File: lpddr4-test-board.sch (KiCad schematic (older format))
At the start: 0 parts

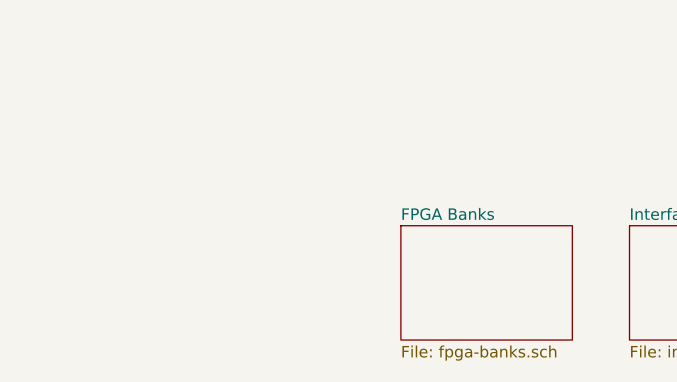
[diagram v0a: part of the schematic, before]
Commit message: Added HyperRAM
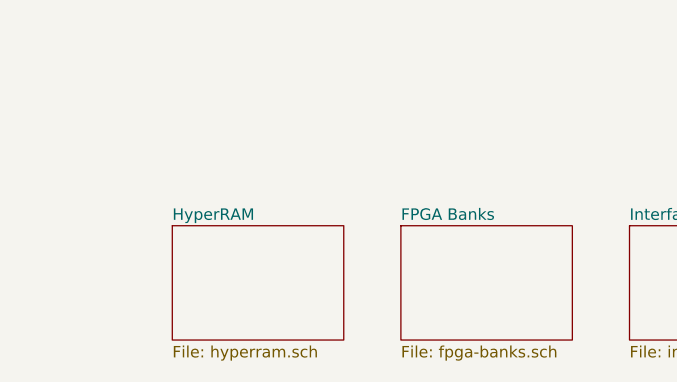
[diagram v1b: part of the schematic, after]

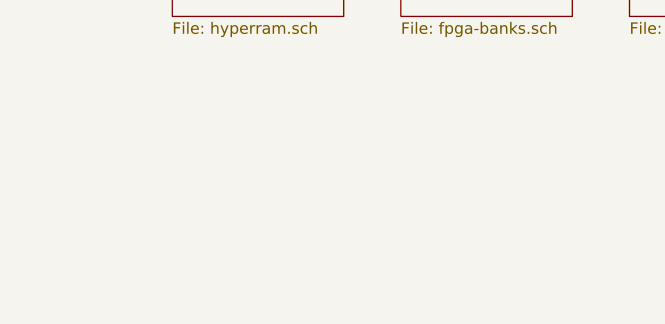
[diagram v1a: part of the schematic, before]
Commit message: Add OSHW logotype
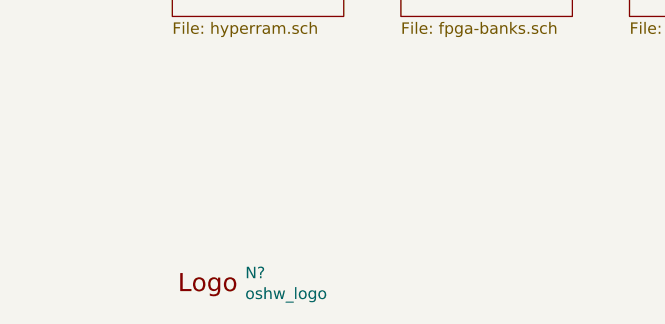
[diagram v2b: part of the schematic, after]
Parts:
- added N?: oshw_logo, antmicro-footprints:oshw-logo, symbol antmicroMechanicalParts:oshw_logo
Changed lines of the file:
@@
 EndData
 $EndBitmap
+$Comp
+L antmicroMechanicalParts:oshw_logo N?
+U 1 1 603B54EA
+P 1400 7000
+F 0 "N?" H 1594 7003 50  0000 L CNN
+F 1 "oshw_logo" H 1594 6912 50  0000 L CNN
+F 2 "antmicro-footprints:oshw-logo" H 1420 6760 50  0001 C CNN
+F 3 "" H 1400 7000 50  0001 C CNN
+	1    1400 7000
+	1    0    0    -1
+$EndComp
 $EndSCHEMATC

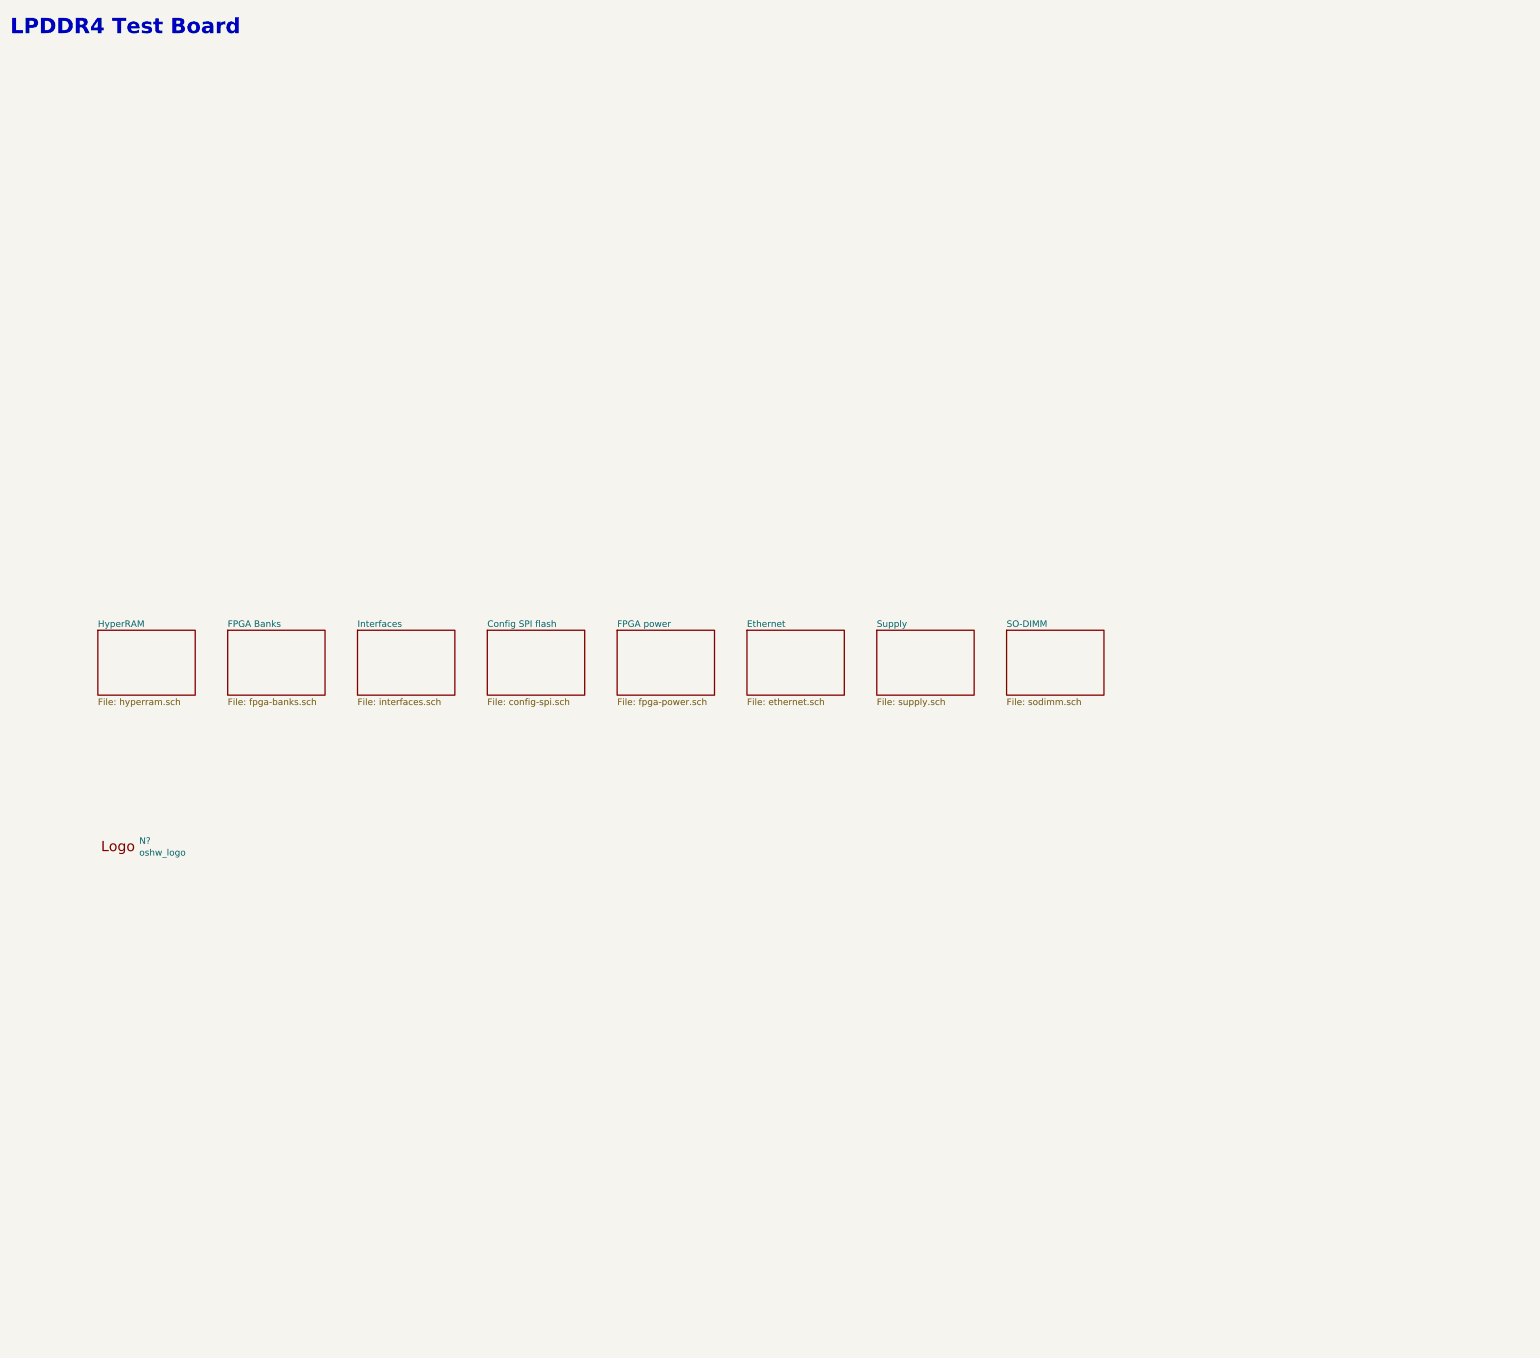
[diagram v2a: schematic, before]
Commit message: Add logotype
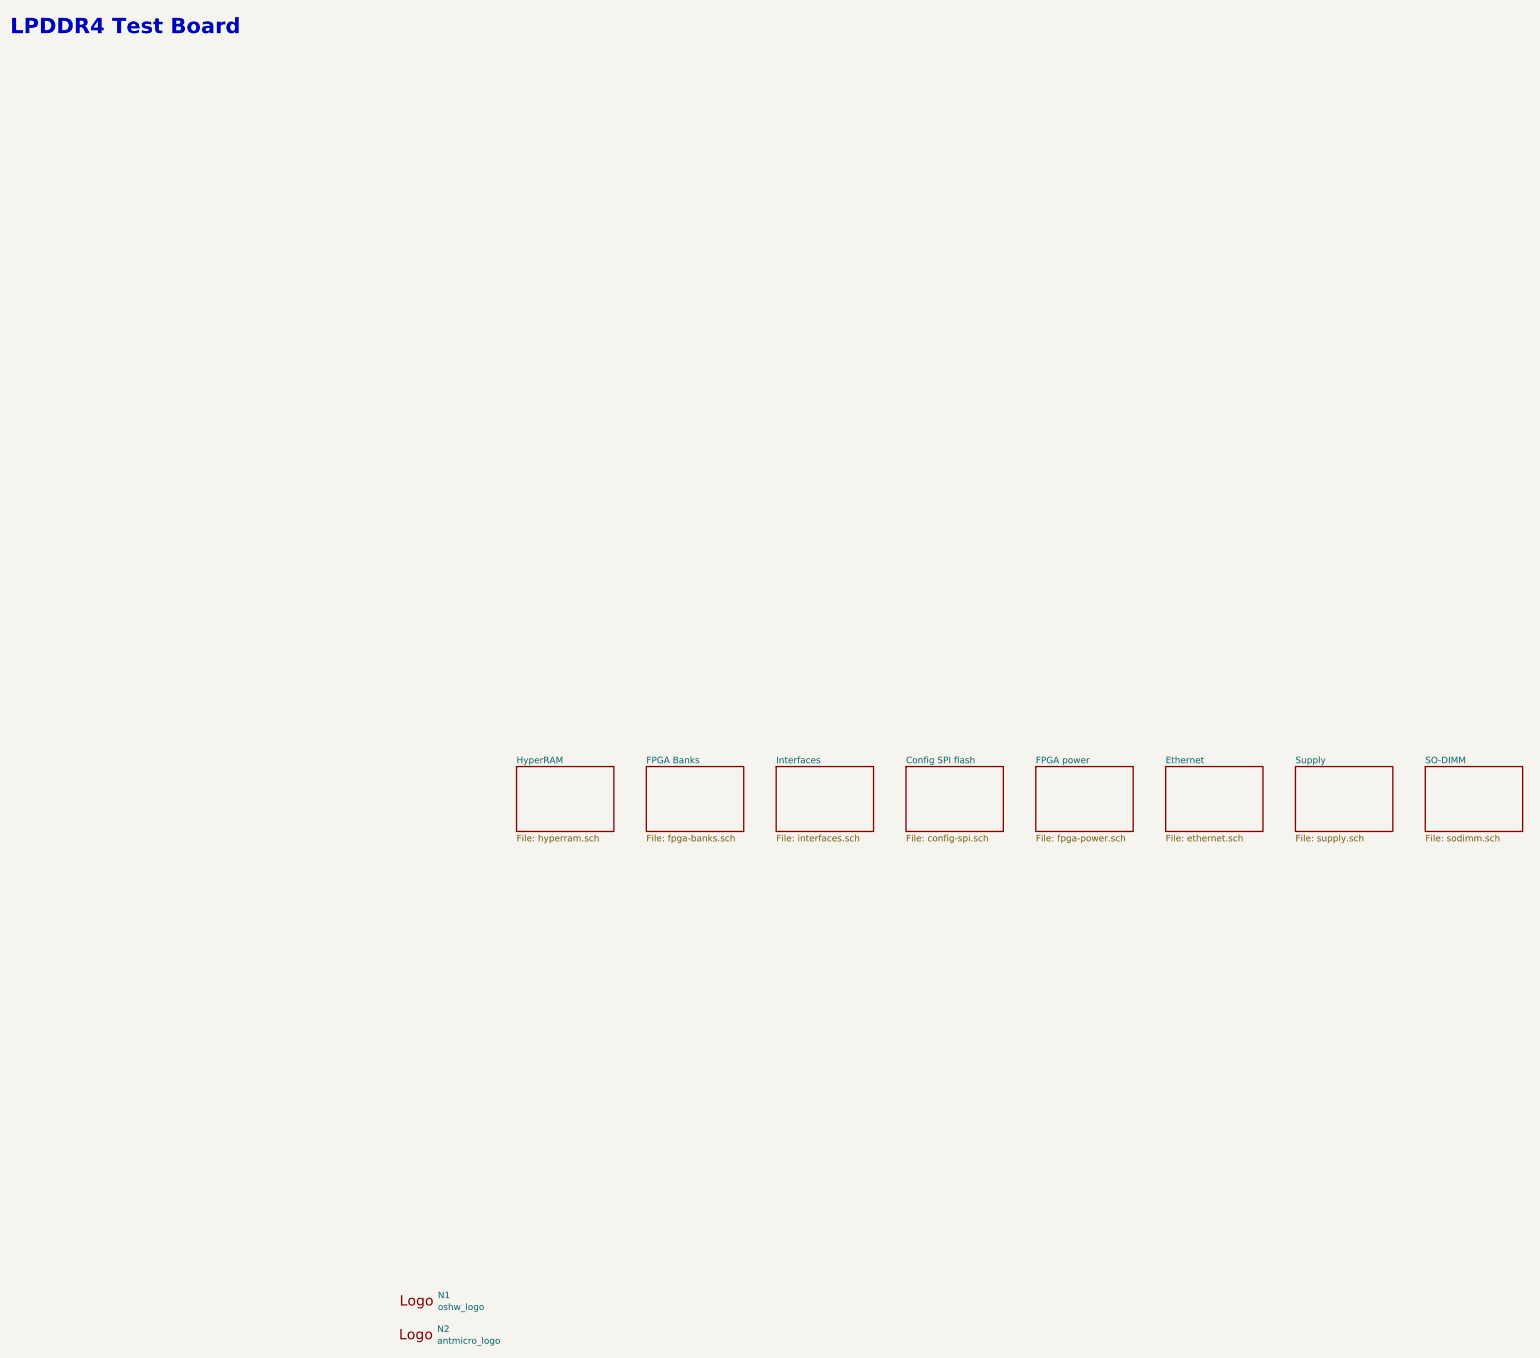
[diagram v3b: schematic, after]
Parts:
- added N2: antmicro_logo, antmicro-footprints:antmicro-logo, symbol antmicroMechanicalParts:antmicro_logo
- gave numbers to parts that had none: 1
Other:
- moved on the sheet: N1
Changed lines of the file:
@@
 EELAYER 30 0
 EELAYER END
-$Descr A4 11693 8268
+$Descr A3 16535 11693
 encoding utf-8
 Sheet 1 9
@@
 $EndDescr
 $Sheet
-S 2275 5375 750  500
+S 5500 6425 750  500
 U 5F96C515
 F0 "FPGA Banks" 50
@@
 $EndSheet
 $Sheet
-S 4275 5375 750  500
+S 7500 6425 750  500
 U 5FD53C7D
 F0 "Config SPI flash" 50
@@
 $EndSheet
 $Sheet
-S 5275 5375 750  500
+S 8500 6425 750  500
 U 600295C1
 F0 "FPGA power" 50
@@
 $EndSheet
 $Sheet
-S 6275 5375 750  500
+S 9500 6425 750  500
 U 5F982999
 F0 "Ethernet" 50
@@
 $EndSheet
 $Sheet
-S 7275 5375 750  500
+S 10500 6425 750  500
 U 60225B0C
 F0 "Supply" 50
@@
 $EndSheet
 $Sheet
-S 3275 5375 750  500
+S 6500 6425 750  500
 U 600E76D8
 F0 "Interfaces" 50
@@
 $EndSheet
 $Sheet
-S 8275 5375 750  500
+S 11500 6425 750  500
 U 5F9FE97C
 F0 "SO-DIMM" 50
@@
 LPDDR4 Test Board
 $Sheet
-S 1275 5375 750  500
+S 4500 6425 750  500
 U 5FEA2994
 F0 "HyperRAM" 50
@@
 $EndSheet
 $Bitmap
-Pos 5900 2700
+Pos 8475 3750
 Scale 1.000000
 Data
@@
 $EndBitmap
 $Comp
-L antmicroMechanicalParts:oshw_logo N?
+L antmicroMechanicalParts:oshw_logo N1
 U 1 1 603B54EA
-P 1400 7000
-F 0 "N?" H 1594 7003 50  0000 L CNN
-F 1 "oshw_logo" H 1594 6912 50  0000 L CNN
-F 2 "antmicro-footprints:oshw-logo" H 1420 6760 50  0001 C CNN
-F 3 "" H 1400 7000 50  0001 C CNN
-	1    1400 7000
+P 3700 10500
+F 0 "N1" H 3894 10503 50  0000 L CNN
+F 1 "oshw_logo" H 3894 10412 50  0000 L CNN
+F 2 "antmicro-footprints:oshw-logo" H 3720 10260 50  0001 C CNN
+F 3 "" H 3700 10500 50  0001 C CNN
+	1    3700 10500
 	1    0    0    -1
 $EndComp
+$Comp
+L antmicroMechanicalParts:antmicro_logo N2
+U 1 1 60405260
+P 3675 10850
+F 0 "N2" H 3889 10943 50  0000 L CNN
+F 1 "antmicro_logo" H 3889 10852 50  0000 L CNN
+F 2 "antmicro-footprints:antmicro-logo" H 3575 11100 50  0001 C CNN
+F 3 "" H 3675 11200 50  0001 C CNN
+	1    3675 10850
+	1    0    0    -1
+$EndComp

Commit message: Update component libraries
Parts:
- N1: footprint antmicro-footprints:oshw-logo -> lpddr4-test-board-footprints:oshw-logo; symbol antmicroMechanicalParts:oshw_logo -> lpddr4-test-board:oshw_logo
- N2: footprint antmicro-footprints:antmicro-logo -> lpddr4-test-board-footprints:antmicro-logo; symbol antmicroMechanicalParts:antmicro_logo -> lpddr4-test-board:antmicro_logo
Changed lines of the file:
@@
 $EndBitmap
 $Comp
-L antmicroMechanicalParts:oshw_logo N1
+L lpddr4-test-board:oshw_logo N1
 U 1 1 603B54EA
 P 3700 10500
 F 0 "N1" H 3894 10503 50  0000 L CNN
 F 1 "oshw_logo" H 3894 10412 50  0000 L CNN
-F 2 "antmicro-footprints:oshw-logo" H 3720 10260 50  0001 C CNN
+F 2 "lpddr4-test-board-footprints:oshw-logo" H 3720 10260 50  0001 C CNN
 F 3 "" H 3700 10500 50  0001 C CNN
 	1    3700 10500
@@
 $EndComp
 $Comp
-L antmicroMechanicalParts:antmicro_logo N2
+L lpddr4-test-board:antmicro_logo N2
 U 1 1 60405260
 P 3675 10850
 F 0 "N2" H 3889 10943 50  0000 L CNN
 F 1 "antmicro_logo" H 3889 10852 50  0000 L CNN
-F 2 "antmicro-footprints:antmicro-logo" H 3575 11100 50  0001 C CNN
+F 2 "lpddr4-test-board-footprints:antmicro-logo" H 3575 11100 50  0001 C CNN
 F 3 "" H 3675 11200 50  0001 C CNN
 	1    3675 10850

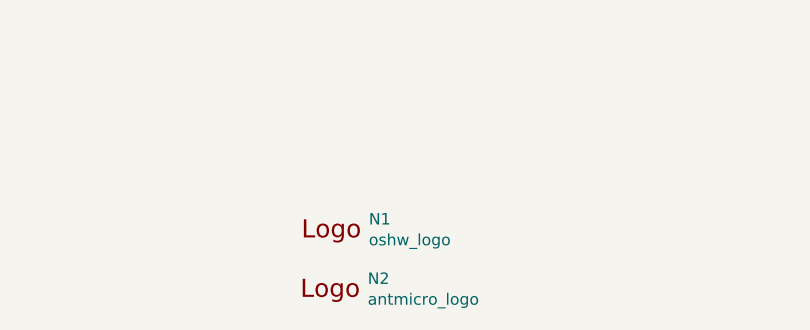
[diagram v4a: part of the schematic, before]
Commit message: Start rev. 1.0.1 Add FAN connector
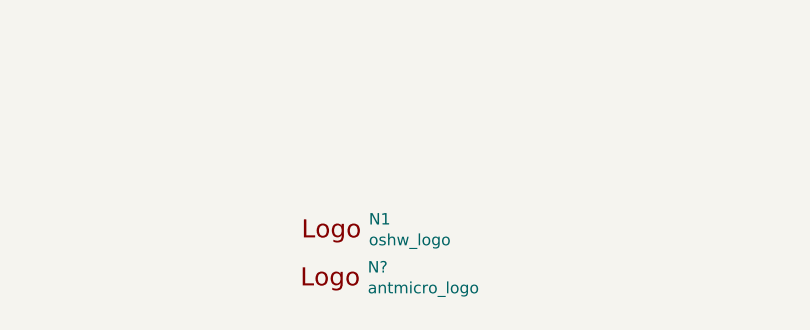
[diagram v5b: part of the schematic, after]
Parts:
- removed N2: antmicro_logo, lpddr4-test-board-footprints:antmicro-logo, symbol lpddr4-test-board:antmicro_logo
- added N?: antmicro_logo, antmicro-footprints:antmicro-logo_scaled_20mm, symbol antmicroMechanicalParts:antmicro_logo
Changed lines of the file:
@@
 Title "LPDDR4 Test Board"
 Date ""
-Rev "1.0.0"
+Rev "1.0.1"
 Comp ""
 Comment1 "LPDDR4 Test Board"
@@
 $EndComp
 $Comp
-L lpddr4-test-board:antmicro_logo N2
-U 1 1 60405260
-P 3675 10850
-F 0 "N2" H 3889 10943 50  0000 L CNN
-F 1 "antmicro_logo" H 3889 10852 50  0000 L CNN
-F 2 "lpddr4-test-board-footprints:antmicro-logo" H 3575 11100 50  0001 C CNN
-F 3 "" H 3675 11200 50  0001 C CNN
-	1    3675 10850
+L antmicroMechanicalParts:antmicro_logo N?
+U 1 1 6003C9B5
+P 3675 10800
+F 0 "N?" H 3889 10893 50  0000 L CNN
+F 1 "antmicro_logo" H 3889 10802 50  0000 L CNN
+F 2 "antmicro-footprints:antmicro-logo_scaled_20mm" H 3575 11050 50  0001 C CNN
+F 3 "" H 3675 11150 50  0001 C CNN
+	1    3675 10800
 	1    0    0    -1
 $EndComp

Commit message: Minor change
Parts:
- gave numbers to parts that had none: 1
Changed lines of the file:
@@
 $EndComp
 $Comp
-L antmicroMechanicalParts:antmicro_logo N?
+L antmicroMechanicalParts:antmicro_logo N2
 U 1 1 6003C9B5
 P 3675 10800
-F 0 "N?" H 3889 10893 50  0000 L CNN
+F 0 "N2" H 3889 10893 50  0000 L CNN
 F 1 "antmicro_logo" H 3889 10802 50  0000 L CNN
 F 2 "antmicro-footprints:antmicro-logo_scaled_20mm" H 3575 11050 50  0001 C CNN
